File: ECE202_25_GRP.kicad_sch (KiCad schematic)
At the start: 8 parts, among them K1 JQC-3FF-009-1Z, K2 JQC-3FF-009-1Z, K3 JQC-3FF-009-1Z, U1 NE555P

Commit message: test update
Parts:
- added K4: JQC-3FF-009-1Z, Relay_THT:Relay_SPDT_Hongfa_JQC-3FF_0XX-1Z, symbol Relay:JQC-3FF-009-1Z
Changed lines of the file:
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@@
+	)
+	(symbol
+		(lib_id "Relay:JQC-3FF-009-1Z")
+		(at 147.32 76.2 0)
+		(unit 1)
+		(exclude_from_sim no)
+		(in_bom yes)
+		(on_board yes)
+		(dnp no)
+		(fields_autoplaced yes)
+		(property "Reference" "K4"
+			(at 158.75 74.9299 0)
+			(effects
+				(font
+					(size 1.27 1.27)
+				)
+				(justify left)
+			)
+		)
+		(property "Value" "JQC-3FF-009-1Z"
+			(at 158.75 77.4699 0)
+			(effects
+				(font
+					(size 1.27 1.27)
+				)
+				(justify left)
+			)
+		)
+		(property "Footprint" "Relay_THT:Relay_SPDT_Hongfa_JQC-3FF_0XX-1Z"
+			(at 158.75 77.47 0)
+			(effects
+				(font
+					(size 1.27 1.27)
+				)
+				(justify left)
+				(hide yes)
+			)
+		)
+		(property "Datasheet" "https://www.digikey.com/htmldatasheets/production/2071105/0/0/1/JQC-3FF.pdf"
+			(at 147.32 76.2 0)
+			(effects
+				(font
+					(size 1.27 1.27)
+				)
+				(hide yes)
+			)
+		)
+		(property "Description" "Subminiature High Power SPDT Relay, 9V Coil nom. 0.36W, 10A switching current, max 10A@277VAC/28VDC"
+			(at 147.32 76.2 0)
+			(effects
+				(font
+					(size 1.27 1.27)
+				)
+				(hide yes)
+			)
+		)
+		(pin "A2"
+		)
+		(pin "A1"
+		)
+		(pin "11"
+		)
+		(pin "12"
+		)
+		(pin "14"
+		)
+		(instances
+			(project ""
+				(path "/17451797-00c3-463e-bda7-94062e36bdd3"
+					(reference "K4")
+					(unit 1)
+				)
+			)
+		)
 	)
 	(symbol

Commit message: Finished V1 of schematic
Screen shot in new images folder
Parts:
- removed K4: JQC-3FF-009-1Z, Relay_THT:Relay_SPDT_Hongfa_JQC-3FF_0XX-1Z, symbol Relay:JQC-3FF-009-1Z
- added C1: 100uF, symbol Device:C
- added J1: Run_in+, symbol Connector:Conn_01x01_Pin
- added J2: Brake_in+, symbol Connector:Conn_01x01_Pin
- added J3: Turn_in+, symbol Connector:Conn_01x01_Pin
- added J4: Run_out+, symbol Connector:Conn_01x01_Pin
- added J5: Brake_out+, symbol Connector:Conn_01x01_Pin
- added J6: Turn_out+, symbol Connector:Conn_01x01_Pin
- added R5: 430, symbol Device:R
- K1: value JQC-3FF-009-1Z -> Running_Relay
- K2: value JQC-3FF-009-1Z -> Turn_Relay
- K3: value JQC-3FF-009-1Z -> Brake_Relay
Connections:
- net GND: now also K1.A2, K2.A2, K3.A2, C1.1
- net at R4.1: now also K3.11
- net at R4.2: no longer K3.14
- net at K2.11: now also R3.1
- net at K2.14: no longer R3.2
- net at K1.11: now also R5.1
- net at U1.6 (THR): no longer R1.2
- now unconnected: R1.1, R2.2, U1.7 (DIS)
- no-connect marks 0 -> 5
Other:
- company: (none) -> HME Designs
- title: (none) -> LED Automotive Lighting Main PCB
- moved on the sheet: R1, R2, R3, R4, U1

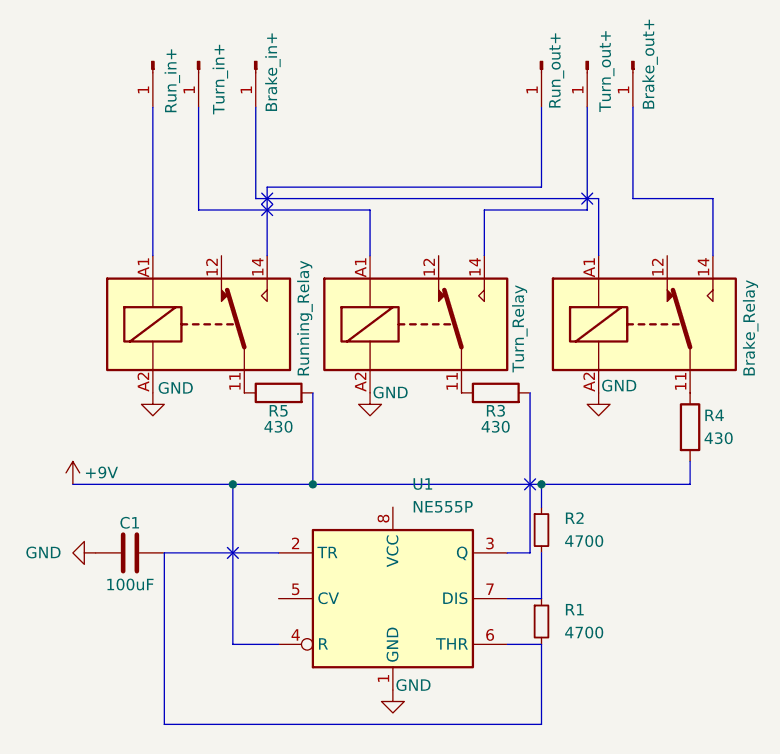
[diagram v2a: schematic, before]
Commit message: Schematic Repairs, v1 PCB
Replaced bus with wires in schematic, added footprints to resistors, caps, pins in schematic.

Imported schematic into PCB, designed PCB.
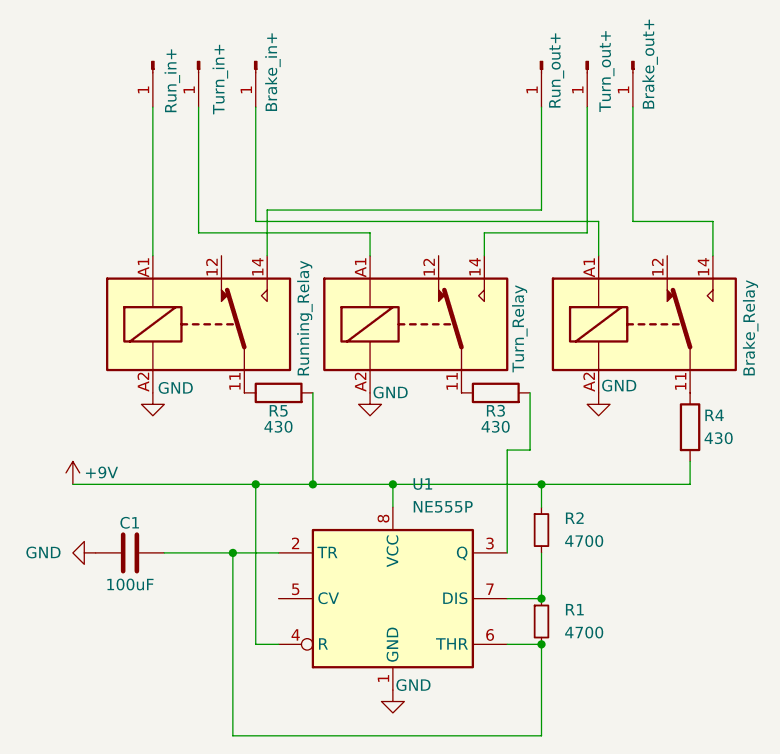
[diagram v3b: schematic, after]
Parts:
- C1: footprint (none) -> Capacitor_SMD:C_1206_3216Metric
- J1, J2, J3, J4, J5, J6: footprint (none) -> Connector_PinHeader_2.54mm:PinHeader_1x01_P2.54mm_Vertical
- R1, R2: footprint (none) -> Resistor_SMD:R_2010_5025Metric
- R3, R4, R5: footprint (none) -> Resistor_SMD:R_0805_2012Metric
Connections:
- net +9V: now also R2.1, R4.2, R5.2, U1.4 (R), U1.8 (VCC)
- net at J5.1 (Pin_1): now also K3.14
- net at J6.1 (Pin_1): now also K2.14
- net at K2.A1: now also J3.1 (Pin_1)
- net at J2.1 (Pin_1): now also K3.A1
- net at K1.14: now also J4.1 (Pin_1)
- net at K1.A1: now also J1.1 (Pin_1)
- net at U1.2 (TR): now also C1.2, R1.2, U1.6 (THR)
- net at U1.3 (Q): now also R3.2
- net at U1.7 (DIS): now also R1.1, R2.2
- no-connect marks 5 -> 0
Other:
- company: HME Designs -> (none)
- title: LED Automotive Lighting Main PCB -> (none)
